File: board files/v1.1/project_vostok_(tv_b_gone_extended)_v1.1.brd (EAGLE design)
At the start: 100 x 44.4 mm, 29 parts, among them IC1 ATMEGA644PV-10PU, IC2 MCP1825S-3302E_DB, Q5 MPS2907A, T1 2N3904, T2 2N3904, T3 2N3904, T4 2N3904, U1 PEC11R-4015F-S0024

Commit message: modify component placements
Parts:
- moved R6 244.5 mm to (69.8, 8.00), flipped to the top, turned to 270 degrees
- moved R5 235.7 mm to (65.8, 8.00), flipped to the top, turned to 270 degrees
- moved LED5 227.1 mm to (24.7, 3.82), flipped to the top, turned to 180 degrees
- moved X1 218.1 mm to (94.8, 25.2), flipped to the top, turned to 180 degrees
- moved R7 216.3 mm to (44.7, 8.00), turned to 90 degrees
- moved R4 209.9 mm to (61.7, 8.00), flipped to the top, turned to 270 degrees
- moved R2 196.4 mm to (53.2, 8.00), flipped to the top, turned to 270 degrees
- moved R3 185.1 mm to (57.2, 8.00), flipped to the top, turned to 270 degrees
- moved R1 184.6 mm to (49.3, 8.00), flipped to the top, turned to 270 degrees
- moved C1 173.2 mm to (54.1, 32.9), flipped to the top
- moved C2 151.8 mm to (54.1, 25.9), flipped to the top
- moved S1 114.2 mm to (77.1, 8.00), turned to 90 degrees
- moved T3 3.44 mm to (14.0, 25.8), flipped to the top, turned to 90 degrees
- moved Q5 2.60 mm to (38.3, 8.00)
- moved T1 2.36 mm to (14.0, 13.8), flipped to the top, turned to 90 degrees
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
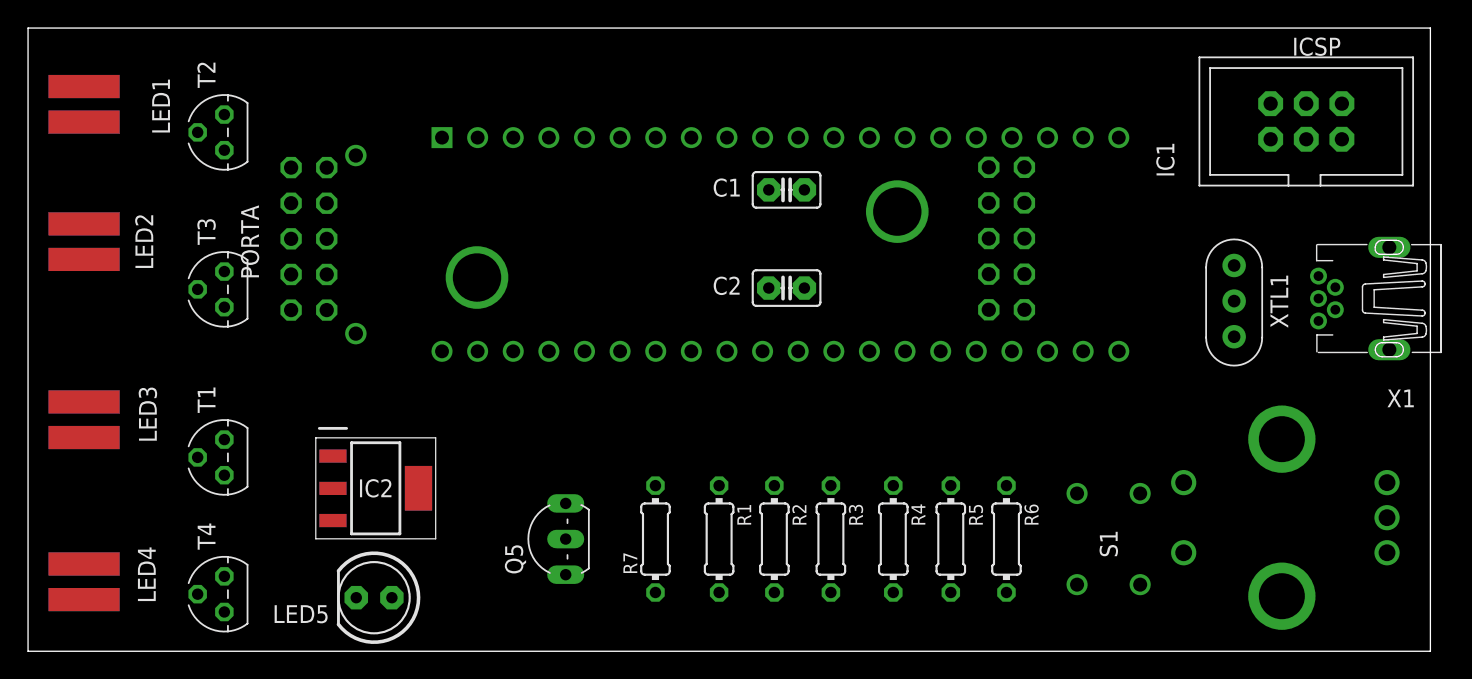
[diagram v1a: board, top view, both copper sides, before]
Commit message: move components and begin wiring
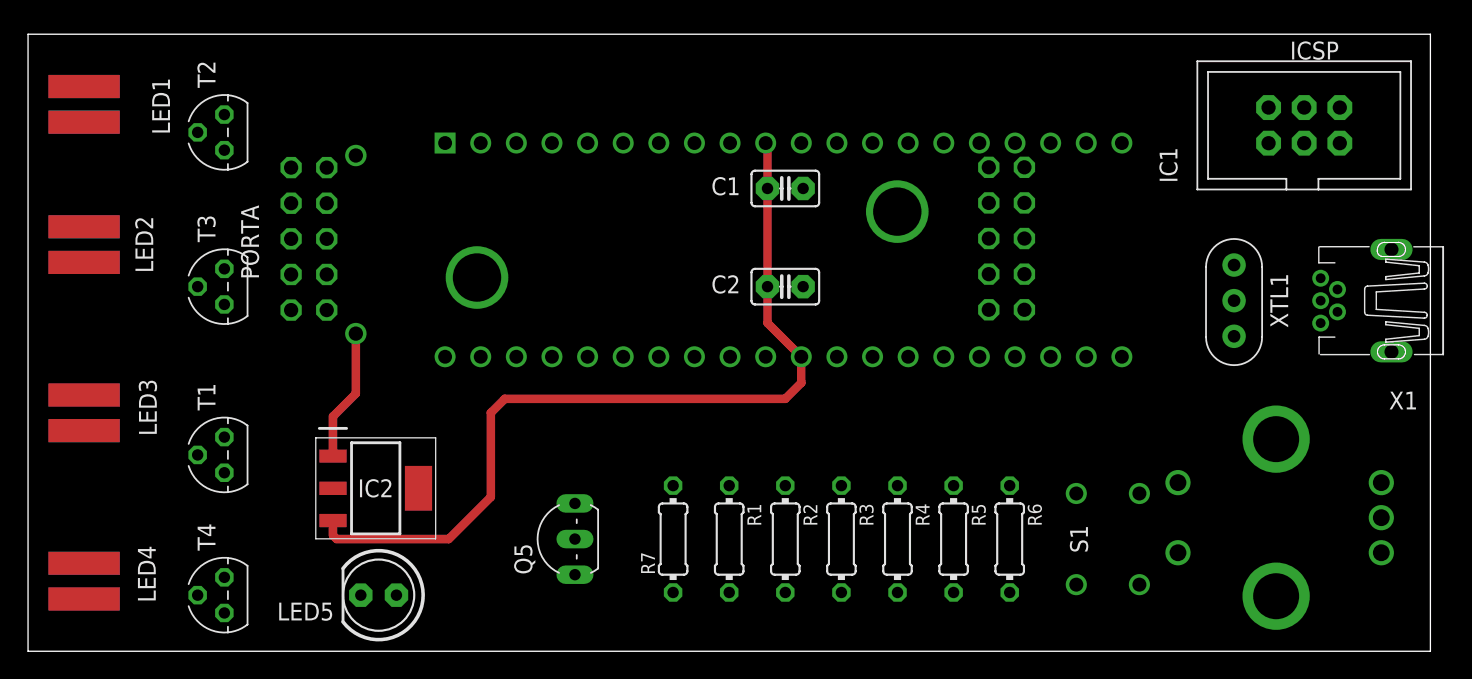
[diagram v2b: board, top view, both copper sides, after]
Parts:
- moved R7 1.26 mm to (46.0, 8.00)
- moved R2 0.78 mm to (54.0, 8.00)
- moved R3 0.75 mm to (58.0, 8.00)
- moved R1 0.72 mm to (50.0, 8.00)
- moved Q5 0.66 mm to (39.0, 8.00)
- moved LED3 0.49 mm to (4.00, 17.0)
- moved IC1 0.45 mm to (78.0, 21.0)
- moved U1 0.41 mm to (89.0, 9.53)
- moved LED5 0.37 mm to (25.0, 4.00)
- moved ICSP 0.32 mm to (91.0, 37.5)
- moved R4 0.30 mm to (62.0, 8.00)
- moved R6 0.23 mm to (70.0, 8.00)
- moved X1 0.22 mm to (95.0, 25.0)
- moved LED2 0.21 mm to (4.00, 29.0)
- moved R5 0.20 mm to (66.0, 8.00)
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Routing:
- net VOUT_REG: track 0.00 -> 60.8 mm
- net VIN_REG: track 0.00 -> 9.41 mm
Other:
- board size 100 x 44.4 mm -> 100 x 44 mm

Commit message: make progress on wiring
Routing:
- net VOUT_REG: track 60.8 -> 139.1 mm
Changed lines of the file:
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@@
 <wire x1="52.73" y1="23.41" x2="52.73" y2="26" width="0.6096" layer="1"/>
 <wire x1="52.73" y1="33" x2="52.73" y2="26" width="0.6096" layer="1"/>
+<wire x1="88.46" y1="38.77" x2="84.37" y2="38.77" width="0.6096" layer="1"/>
+<wire x1="84.37" y1="38.77" x2="80.1" y2="34.5" width="0.6096" layer="1"/>
+<wire x1="80.1" y1="34.5" x2="75" y2="34.5" width="0.6096" layer="1"/>
+<wire x1="75" y1="34.5" x2="71.06" y2="34.5" width="0.6096" layer="1"/>
+<wire x1="71.06" y1="34.5" x2="71.05" y2="34.51" width="0.6096" layer="1"/>
+<wire x1="84.37" y1="38.77" x2="84.37" y2="38.77" width="0.6096" layer="1"/>
+<wire x1="84.37" y1="38.77" x2="84.37" y2="38.77" width="0.6096" layer="1"/>
+<wire x1="84.37" y1="38.77" x2="55" y2="38.77" width="0.6096" layer="1"/>
+<wire x1="55" y1="38.77" x2="54.77" y2="38.77" width="0.6096" layer="1"/>
 <wire x1="52.6" y1="36.24" x2="52.73" y2="36.11" width="0.6096" layer="1"/>
 <wire x1="52.73" y1="36.11" x2="52.73" y2="33" width="0.6096" layer="1"/>
-<wire x1="71.05" y1="34.51" x2="88.46" y2="38.77" width="0" layer="19" extent="1-1"/>
-<wire x1="52.73" y1="36.11" x2="71.05" y2="34.51" width="0" layer="19" extent="1-1"/>
-<wire x1="58" y1="11.81" x2="54" y2="18" width="0" layer="19" extent="1-1"/>
+<wire x1="55" y1="38.77" x2="53.77" y2="38.77" width="0.6096" layer="1"/>
+<wire x1="52.6" y1="37.6" x2="52.6" y2="36.24" width="0.6096" layer="1"/>
+<wire x1="53.77" y1="38.77" x2="52.6" y2="37.6" width="0.6096" layer="1"/>
+<wire x1="21.299640625" y1="34.488059375" x2="26" y2="29.7877" width="0.6096" layer="1"/>
+<wire x1="26" y1="29.7877" x2="26" y2="19" width="0.6096" layer="1"/>
+<wire x1="26" y1="19" x2="28" y2="17" width="0.6096" layer="1"/>
+<wire x1="28" y1="17" x2="33" y2="17" width="0.6096" layer="1"/>
+<wire x1="54" y1="18" x2="58" y2="11.81" width="0" layer="19" extent="1-1"/>
 <wire x1="39" y1="5.46" x2="33" y2="11" width="0" layer="19" extent="1-1"/>
 <wire x1="62" y1="4.19" x2="58" y2="11.81" width="0" layer="19" extent="1-1"/>
 <wire x1="50" y1="4.19" x2="58" y2="11.81" width="0" layer="19" extent="1-1"/>
-<wire x1="21.299640625" y1="34.488059375" x2="34" y2="18" width="0" layer="19" extent="1-1"/>
 </signal>
 <signal name="PD1">

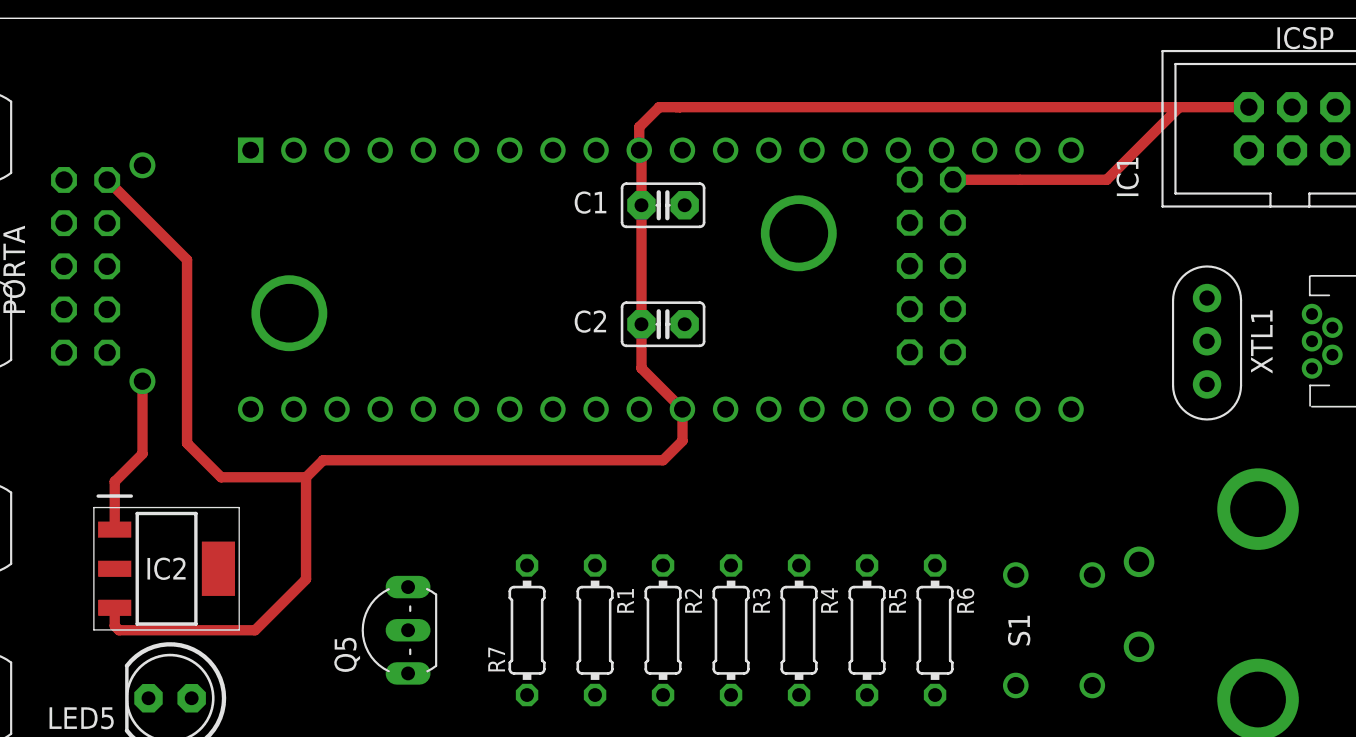
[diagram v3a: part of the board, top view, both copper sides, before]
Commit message: ripup traces for movement of components
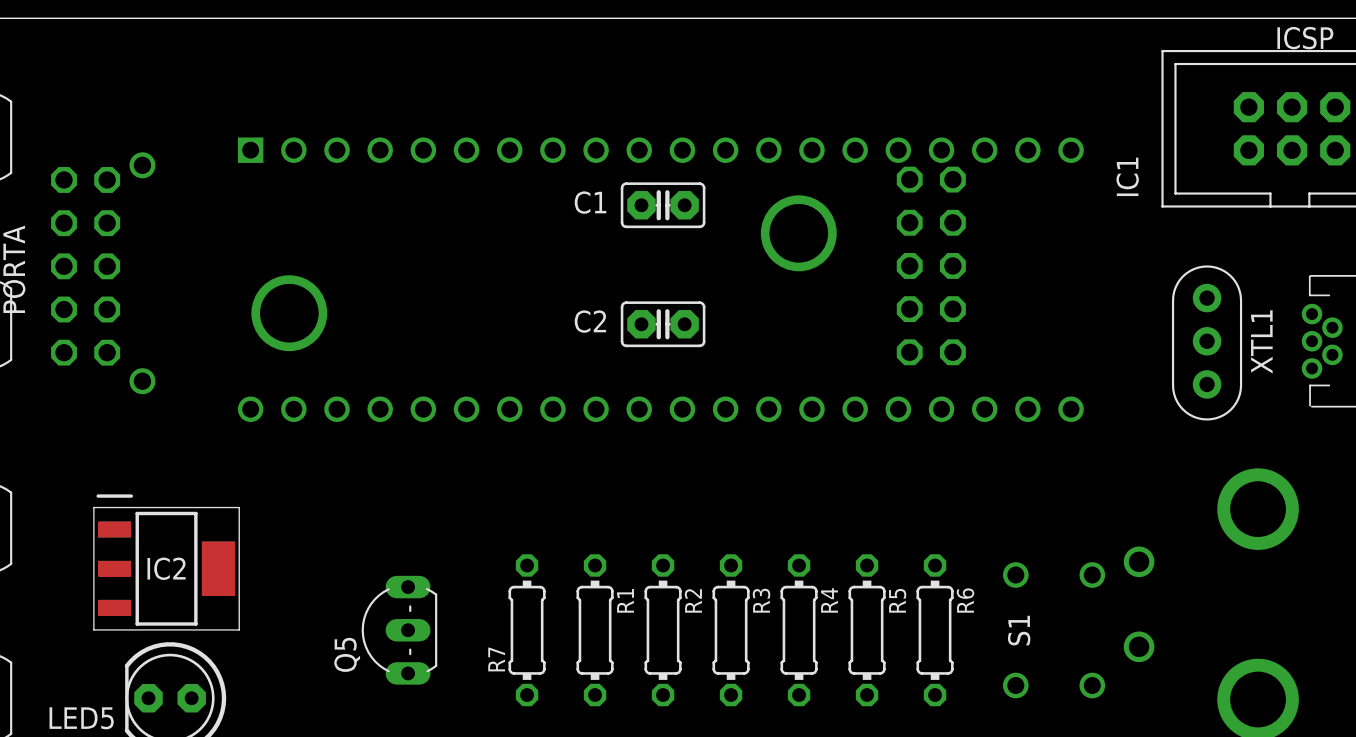
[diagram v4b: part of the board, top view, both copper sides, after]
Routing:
- net VOUT_REG: track 139.1 -> 0.00 mm
- net VIN_REG: track 9.41 -> 0.00 mm

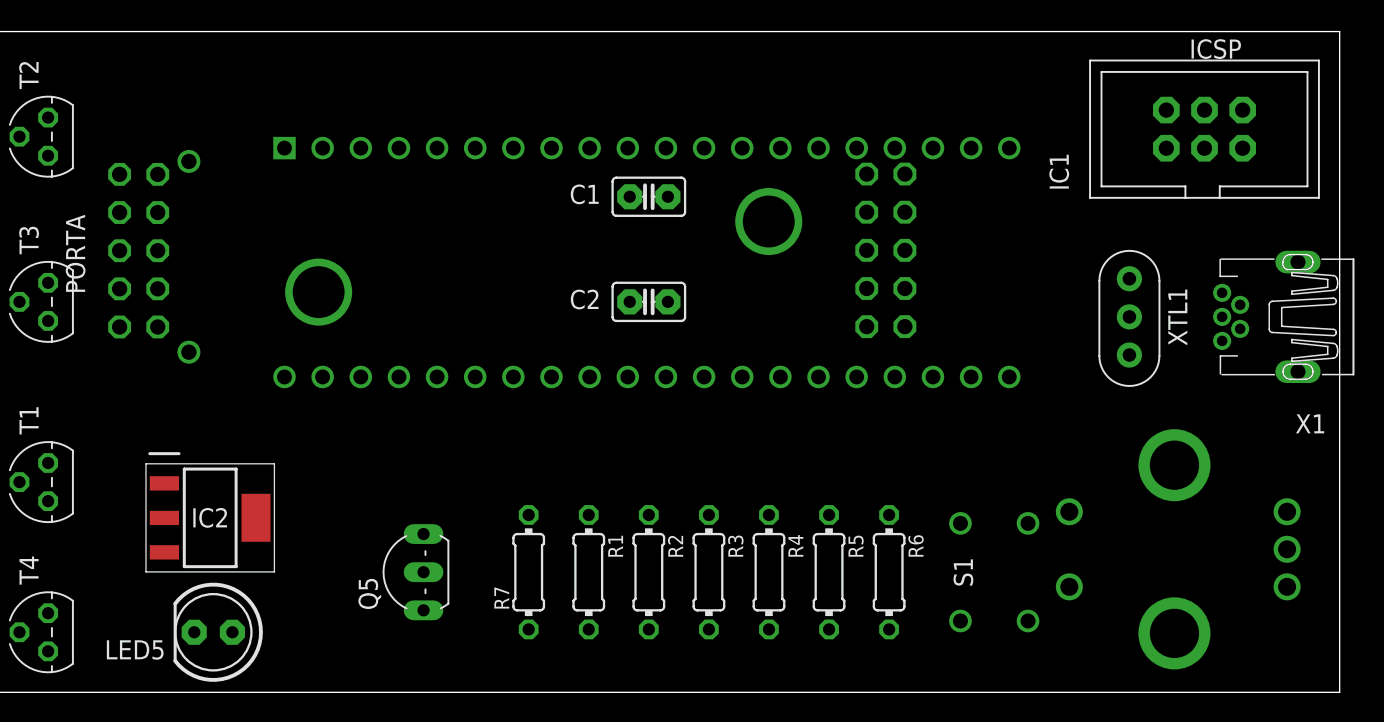
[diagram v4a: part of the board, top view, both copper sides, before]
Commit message: modify component positions on board
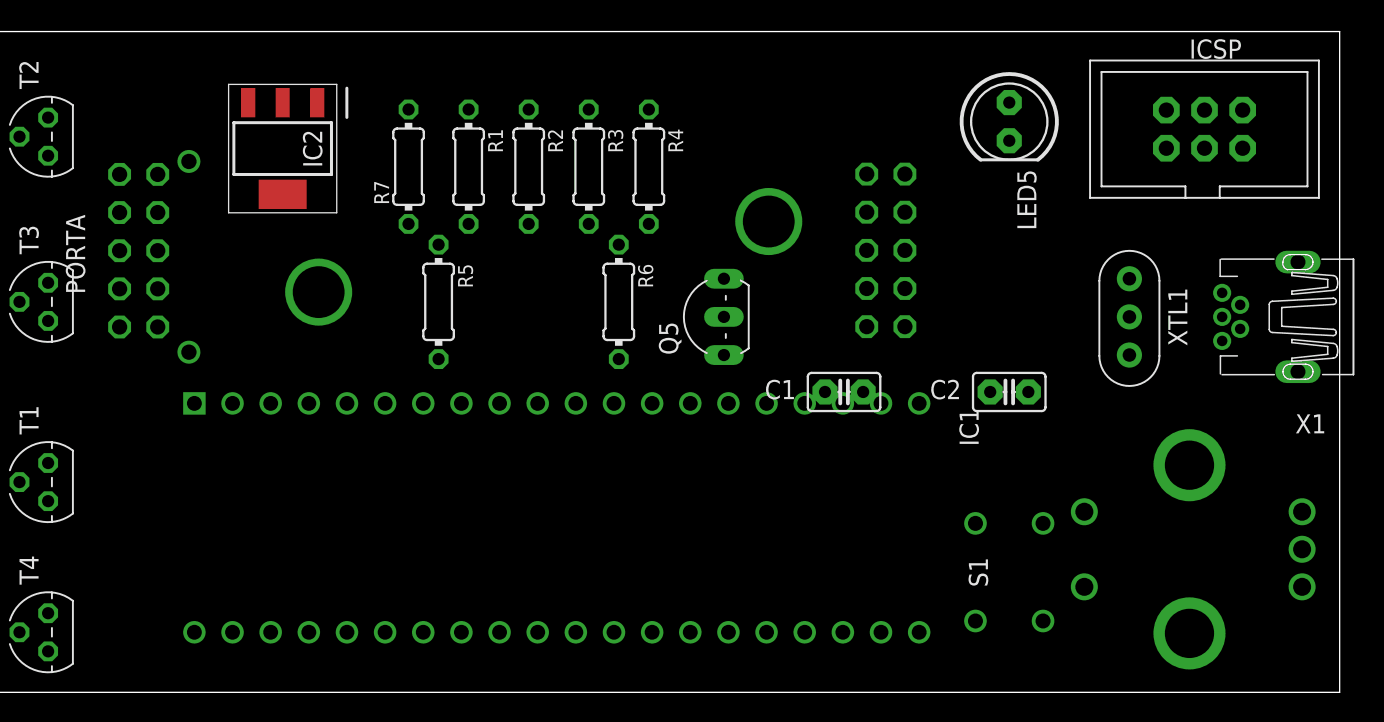
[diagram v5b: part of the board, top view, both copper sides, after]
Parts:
- moved LED5 63.0 mm to (78.0, 38.0), turned to 270 degrees
- moved R5 31.6 mm to (40.0, 26.0)
- moved R1 28.2 mm to (42.0, 35.0)
- moved R2 28.2 mm to (46.0, 35.0)
- moved R3 28.2 mm to (50.0, 35.0)
- moved R4 28.2 mm to (54.0, 35.0)
- moved R7 28.2 mm to (38.0, 35.0)
- moved Q5 26.2 mm to (59.0, 25.0)
- moved R6 25.5 mm to (52.0, 26.0)
- moved IC2 25.1 mm to (29.6, 36.2), turned to 270 degrees
- moved C2 24.7 mm to (78.0, 20.0)
- moved C1 18.4 mm to (67.0, 20.0)
- moved IC1 18.0 mm to (72.0, 4.00)
- moved S1 1.00 mm to (78.0, 8.00)
- moved U1 1.00 mm to (90.0, 9.53)

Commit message: tidy labels on board
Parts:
- moved C2 35.0 mm to (48.0, 2.00)
- moved C1 20.4 mm to (47.0, 24.0)
- moved R6 16.1 mm to (60.0, 40.0), turned to 0 degrees
- moved R5 12.8 mm to (50.0, 34.0), turned to 0 degrees
- moved R2 6.08 mm to (40.0, 34.0), turned to 0 degrees
- moved R7 5.39 mm to (40.0, 40.0), turned to 180 degrees
- moved R3 5.00 mm to (50.0, 40.0), turned to 0 degrees
- moved R4 4.47 mm to (50.0, 37.0), turned to 0 degrees
- moved R1 2.83 mm to (40.0, 37.0), turned to 0 degrees
- moved IC1 1.00 mm to (72.0, 5.00)
- moved IC2 0.88 mm to (30.0, 37.0)
